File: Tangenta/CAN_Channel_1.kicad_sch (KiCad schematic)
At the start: 21 parts, among them J22 Conn_01x02_Pin, Q3 BSS138, U20 ADM3053

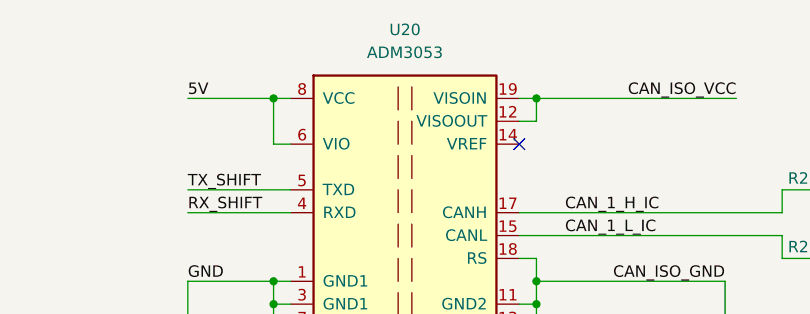
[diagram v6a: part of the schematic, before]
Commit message: Re-annotated. Ready for JLCPCB design verification.
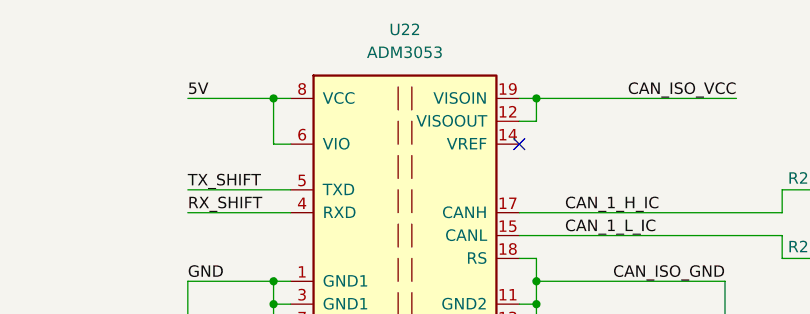
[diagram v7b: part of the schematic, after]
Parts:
- renumbered U20 to U22
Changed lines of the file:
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@@
         )
         (path "/358d1bcf-7599-4352-8c4d-baa18a5f09e6/b5394a48-5ef8-44c9-9d56-604d4ce6d7c8/96e01dc6-7803-4642-812e-1845a7add5da"
-          (reference "C189") (unit 1)
+          (reference "C199") (unit 1)
         )
       )
@@
         )
         (path "/358d1bcf-7599-4352-8c4d-baa18a5f09e6/b5394a48-5ef8-44c9-9d56-604d4ce6d7c8/96e01dc6-7803-4642-812e-1845a7add5da"
-          (reference "#PWR088") (unit 1)
+          (reference "#PWR094") (unit 1)
         )
       )
@@
         )
         (path "/358d1bcf-7599-4352-8c4d-baa18a5f09e6/b5394a48-5ef8-44c9-9d56-604d4ce6d7c8/96e01dc6-7803-4642-812e-1845a7add5da"
-          (reference "C195") (unit 1)
+          (reference "C202") (unit 1)
         )
       )
@@
         )
         (path "/358d1bcf-7599-4352-8c4d-baa18a5f09e6/b5394a48-5ef8-44c9-9d56-604d4ce6d7c8/96e01dc6-7803-4642-812e-1845a7add5da"
-          (reference "C188") (unit 1)
+          (reference "C197") (unit 1)
         )
       )
@@
         )
         (path "/358d1bcf-7599-4352-8c4d-baa18a5f09e6/b5394a48-5ef8-44c9-9d56-604d4ce6d7c8/96e01dc6-7803-4642-812e-1845a7add5da"
-          (reference "C191") (unit 1)
+          (reference "C200") (unit 1)
         )
       )
@@
         )
         (path "/358d1bcf-7599-4352-8c4d-baa18a5f09e6/b5394a48-5ef8-44c9-9d56-604d4ce6d7c8/96e01dc6-7803-4642-812e-1845a7add5da"
-          (reference "Q15") (unit 1)
+          (reference "Q19") (unit 1)
         )
       )
@@
         )
         (path "/358d1bcf-7599-4352-8c4d-baa18a5f09e6/b5394a48-5ef8-44c9-9d56-604d4ce6d7c8/96e01dc6-7803-4642-812e-1845a7add5da"
-          (reference "R151") (unit 1)
+          (reference "R190") (unit 1)
         )
       )
@@
         )
         (path "/358d1bcf-7599-4352-8c4d-baa18a5f09e6/b5394a48-5ef8-44c9-9d56-604d4ce6d7c8/96e01dc6-7803-4642-812e-1845a7add5da"
-          (reference "C193") (unit 1)
+          (reference "C201") (unit 1)
         )
       )
@@
         )
         (path "/358d1bcf-7599-4352-8c4d-baa18a5f09e6/b5394a48-5ef8-44c9-9d56-604d4ce6d7c8/96e01dc6-7803-4642-812e-1845a7add5da"
-          (reference "C192") (unit 1)
+          (reference "C203") (unit 1)
         )
       )
@@
         )
         (path "/358d1bcf-7599-4352-8c4d-baa18a5f09e6/b5394a48-5ef8-44c9-9d56-604d4ce6d7c8/96e01dc6-7803-4642-812e-1845a7add5da"
-          (reference "J23") (unit 1)
+          (reference "J32") (unit 1)
         )
       )
@@
         )
         (path "/358d1bcf-7599-4352-8c4d-baa18a5f09e6/b5394a48-5ef8-44c9-9d56-604d4ce6d7c8/96e01dc6-7803-4642-812e-1845a7add5da"
-          (reference "Q16") (unit 1)
+          (reference "Q20") (unit 1)
         )
       )
@@
         )
         (path "/358d1bcf-7599-4352-8c4d-baa18a5f09e6/b5394a48-5ef8-44c9-9d56-604d4ce6d7c8/96e01dc6-7803-4642-812e-1845a7add5da"
-          (reference "#PWR086") (unit 1)
+          (reference "#PWR093") (unit 1)
         )
       )
@@
         )
         (path "/358d1bcf-7599-4352-8c4d-baa18a5f09e6/b5394a48-5ef8-44c9-9d56-604d4ce6d7c8/96e01dc6-7803-4642-812e-1845a7add5da"
-          (reference "C190") (unit 1)
+          (reference "C198") (unit 1)
         )
       )
@@
         )
         (path "/358d1bcf-7599-4352-8c4d-baa18a5f09e6/b5394a48-5ef8-44c9-9d56-604d4ce6d7c8/96e01dc6-7803-4642-812e-1845a7add5da"
-          (reference "R177") (unit 1)
+          (reference "R189") (unit 1)
         )
       )
@@
         )
         (path "/358d1bcf-7599-4352-8c4d-baa18a5f09e6/b5394a48-5ef8-44c9-9d56-604d4ce6d7c8/96e01dc6-7803-4642-812e-1845a7add5da"
-          (reference "#PWR087") (unit 1)
+          (reference "#PWR092") (unit 1)
         )
       )
@@
         )
         (path "/358d1bcf-7599-4352-8c4d-baa18a5f09e6/b5394a48-5ef8-44c9-9d56-604d4ce6d7c8/96e01dc6-7803-4642-812e-1845a7add5da"
-          (reference "R168") (unit 1)
+          (reference "R191") (unit 1)
         )
       )
@@
         )
         (path "/358d1bcf-7599-4352-8c4d-baa18a5f09e6/b5394a48-5ef8-44c9-9d56-604d4ce6d7c8/96e01dc6-7803-4642-812e-1845a7add5da"
-          (reference "R175") (unit 1)
+          (reference "R187") (unit 1)
         )
       )
@@
         )
         (path "/358d1bcf-7599-4352-8c4d-baa18a5f09e6/b5394a48-5ef8-44c9-9d56-604d4ce6d7c8/96e01dc6-7803-4642-812e-1845a7add5da"
-          (reference "C194") (unit 1)
+          (reference "C204") (unit 1)
         )
       )
@@
         )
         (path "/358d1bcf-7599-4352-8c4d-baa18a5f09e6/b5394a48-5ef8-44c9-9d56-604d4ce6d7c8/96e01dc6-7803-4642-812e-1845a7add5da"
-          (reference "#PWR083") (unit 1)
+          (reference "#PWR091") (unit 1)
         )
       )
@@
         )
         (path "/358d1bcf-7599-4352-8c4d-baa18a5f09e6/b5394a48-5ef8-44c9-9d56-604d4ce6d7c8/96e01dc6-7803-4642-812e-1845a7add5da"
-          (reference "R176") (unit 1)
+          (reference "R188") (unit 1)
         )
       )
@@
         )
         (path "/358d1bcf-7599-4352-8c4d-baa18a5f09e6/b5394a48-5ef8-44c9-9d56-604d4ce6d7c8/96e01dc6-7803-4642-812e-1845a7add5da"
-          (reference "R184") (unit 1)
+          (reference "R192") (unit 1)
         )
       )
@@
   (symbol (lib_id "CholaSymbolsPrjLib:ADM3053") (at 137.16 74.93 0) (unit 1)
     (in_bom yes) (on_board yes) (dnp no) (fields_autoplaced)
-    (property "Reference" "U20" (at 137.16 52.07 0)
+    (property "Reference" "U22" (at 137.16 52.07 0)
       (effects (font (size 1.27 1.27)))
     )
@@
       (project "Tangenta"
         (path "/358d1bcf-7599-4352-8c4d-baa18a5f09e6/b5394a48-5ef8-44c9-9d56-604d4ce6d7c8/96e01dc6-7803-4642-812e-1845a7add5da"
-          (reference "U20") (unit 1)
+          (reference "U22") (unit 1)
         )
       )
@@
         )
         (path "/358d1bcf-7599-4352-8c4d-baa18a5f09e6/b5394a48-5ef8-44c9-9d56-604d4ce6d7c8/96e01dc6-7803-4642-812e-1845a7add5da"
-          (reference "R174") (unit 1)
-        )
-      )
+          (reference "R186") (unit 1)
+        )
+      )

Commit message: ...
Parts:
- C1: symbol CholaSymbolsPrjLib:C_Small -> LocalPrjLib:C_Small
- FB1: symbol CholaSymbolsPrjLib:GZ2012D101TF -> LocalPrjLib:GZ2012D101TF
- J22: symbol CholaSymbolsPrjLib:Conn_01x02_Pin -> LocalPrjLib:Conn_01x02_Pin
- Q3: symbol CholaSymbolsPrjLib:BSS138 -> LocalPrjLib:BSS138
- R2, R4: symbol CholaSymbolsPrjLib:R_Small_US -> LocalPrjLib:R_Small_US
- U22: symbol CholaSymbolsPrjLib:ADM3053 -> LocalPrjLib:ADM3053
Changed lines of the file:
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@@
     (effects (font (size 1.27 1.27)) (justify left))
   )
-  (symbol (lib_id "CholaSymbolsPrjLib:GZ2012D101TF") (at 168.91 140.97 0) (unit 1)
+  (symbol (lib_id "LocalPrjLib:GZ2012D101TF") (at 168.91 140.97 0) (unit 1)
     (in_bom yes) (on_board yes) (dnp no)
     (property "Reference" "FB1" (at 168.91 138.43 0)
@@
     )
   )
-  (symbol (lib_id "CholaSymbolsPrjLib:C_Small") (at 132.08 116.84 180) (unit 1)
+  (symbol (lib_id "LocalPrjLib:C_Small") (at 132.08 116.84 180) (unit 1)
     (in_bom yes) (on_board yes) (dnp no)
     (property "Reference" "C1" (at 129.5399 114.9349 0)
@@
     )
   )
-  (symbol (lib_id "CholaSymbolsPrjLib:C_Small") (at 159.385 135.89 0) (mirror x) (unit 1)
+  (symbol (lib_id "LocalPrjLib:C_Small") (at 159.385 135.89 0) (mirror x) (unit 1)
     (in_bom yes) (on_board yes) (dnp no)
     (property "Reference" "C1" (at 161.9251 133.9849 0)
@@
     )
   )
-  (symbol (lib_id "CholaSymbolsPrjLib:C_Small") (at 124.46 116.84 180) (unit 1)
+  (symbol (lib_id "LocalPrjLib:C_Small") (at 124.46 116.84 180) (unit 1)
     (in_bom yes) (on_board yes) (dnp no)
     (property "Reference" "C1" (at 121.9199 114.9349 0)
@@
     )
   )
-  (symbol (lib_id "CholaSymbolsPrjLib:C_Small") (at 132.08 135.89 180) (unit 1)
+  (symbol (lib_id "LocalPrjLib:C_Small") (at 132.08 135.89 180) (unit 1)
     (in_bom yes) (on_board yes) (dnp no)
     (property "Reference" "C1" (at 129.5399 133.9849 0)
@@
     )
   )
-  (symbol (lib_id "CholaSymbolsPrjLib:BSS138") (at 66.04 117.475 270) (unit 1)
+  (symbol (lib_id "LocalPrjLib:BSS138") (at 66.04 117.475 270) (unit 1)
     (in_bom yes) (on_board yes) (dnp no)
     (property "Reference" "Q3" (at 68.58 114.935 90)
@@
     )
   )
-  (symbol (lib_id "CholaSymbolsPrjLib:R_Small_US") (at 186.69 69.85 270) (unit 1)
+  (symbol (lib_id "LocalPrjLib:R_Small_US") (at 186.69 69.85 270) (unit 1)
     (in_bom yes) (on_board yes) (dnp no)
     (property "Reference" "R2" (at 179.705 68.58 90)
@@
     )
   )
-  (symbol (lib_id "CholaSymbolsPrjLib:C_Small") (at 141.605 116.84 0) (mirror x) (unit 1)
+  (symbol (lib_id "LocalPrjLib:C_Small") (at 141.605 116.84 0) (mirror x) (unit 1)
     (in_bom yes) (on_board yes) (dnp no)
     (property "Reference" "C1" (at 144.1451 114.9349 0)
@@
     )
   )
-  (symbol (lib_id "CholaSymbolsPrjLib:C_Small") (at 160.655 116.84 0) (mirror x) (unit 1)
+  (symbol (lib_id "LocalPrjLib:C_Small") (at 160.655 116.84 0) (mirror x) (unit 1)
     (in_bom yes) (on_board yes) (dnp no)
     (property "Reference" "C1" (at 163.1951 114.9349 0)
@@
     )
   )
-  (symbol (lib_id "CholaSymbolsPrjLib:Conn_01x02_Pin") (at 139.065 153.67 270) (unit 1)
+  (symbol (lib_id "LocalPrjLib:Conn_01x02_Pin") (at 139.065 153.67 270) (unit 1)
     (in_bom yes) (on_board yes) (dnp no)
     (property "Reference" "J22" (at 135.89 152.4 90)
@@
     )
   )
-  (symbol (lib_id "CholaSymbolsPrjLib:BSS138") (at 66.04 138.43 270) (unit 1)
+  (symbol (lib_id "LocalPrjLib:BSS138") (at 66.04 138.43 270) (unit 1)
     (in_bom yes) (on_board yes) (dnp no)
     (property "Reference" "Q3" (at 68.58 135.89 90)
@@
     )
   )
-  (symbol (lib_id "CholaSymbolsPrjLib:C_Small") (at 124.46 135.89 180) (unit 1)
+  (symbol (lib_id "LocalPrjLib:C_Small") (at 124.46 135.89 180) (unit 1)
     (in_bom yes) (on_board yes) (dnp no)
     (property "Reference" "C1" (at 121.9199 133.9849 0)
@@
     )
   )
-  (symbol (lib_id "CholaSymbolsPrjLib:R_Small_US") (at 80.01 134.62 180) (unit 1)
+  (symbol (lib_id "LocalPrjLib:R_Small_US") (at 80.01 134.62 180) (unit 1)
     (in_bom yes) (on_board yes) (dnp no)
     (property "Reference" "R2" (at 78.74 133.35 0)
@@
     )
   )
-  (symbol (lib_id "CholaSymbolsPrjLib:R_Small_US") (at 186.69 77.47 270) (unit 1)
+  (symbol (lib_id "LocalPrjLib:R_Small_US") (at 186.69 77.47 270) (unit 1)
     (in_bom yes) (on_board yes) (dnp no)
     (property "Reference" "R2" (at 179.705 76.2 90)
@@
     )
   )
-  (symbol (lib_id "CholaSymbolsPrjLib:R_Small_US") (at 53.34 134.62 180) (unit 1)
+  (symbol (lib_id "LocalPrjLib:R_Small_US") (at 53.34 134.62 180) (unit 1)
     (in_bom yes) (on_board yes) (dnp no)
     (property "Reference" "R2" (at 52.07 133.35 0)
@@
     )
   )
-  (symbol (lib_id "CholaSymbolsPrjLib:C_Small") (at 178.435 135.89 0) (mirror x) (unit 1)
+  (symbol (lib_id "LocalPrjLib:C_Small") (at 178.435 135.89 0) (mirror x) (unit 1)
     (in_bom yes) (on_board yes) (dnp no)
     (property "Reference" "C1" (at 180.9751 133.9849 0)
@@
     )
   )
-  (symbol (lib_id "CholaSymbolsPrjLib:R_Small_US") (at 80.01 113.665 180) (unit 1)
+  (symbol (lib_id "LocalPrjLib:R_Small_US") (at 80.01 113.665 180) (unit 1)
     (in_bom yes) (on_board yes) (dnp no)
     (property "Reference" "R2" (at 78.74 112.395 0)
@@
     )
   )
-  (symbol (lib_id "CholaSymbolsPrjLib:R_Small_US") (at 193.675 73.66 0) (unit 1)
+  (symbol (lib_id "LocalPrjLib:R_Small_US") (at 193.675 73.66 0) (unit 1)
     (in_bom yes) (on_board yes) (dnp no)
     (property "Reference" "R4" (at 197.485 72.39 0)
@@
     )
   )
-  (symbol (lib_id "CholaSymbolsPrjLib:ADM3053") (at 137.16 74.93 0) (unit 1)
+  (symbol (lib_id "LocalPrjLib:ADM3053") (at 137.16 74.93 0) (unit 1)
     (in_bom yes) (on_board yes) (dnp no) (fields_autoplaced)
     (property "Reference" "U22" (at 137.16 52.07 0)
@@
     )
   )
-  (symbol (lib_id "CholaSymbolsPrjLib:R_Small_US") (at 53.34 113.665 180) (unit 1)
+  (symbol (lib_id "LocalPrjLib:R_Small_US") (at 53.34 113.665 180) (unit 1)
     (in_bom yes) (on_board yes) (dnp no)
     (property "Reference" "R2" (at 52.07 112.395 0)
@@
     )
   )
-  (symbol (lib_id "CholaSymbolsPrjLib:GZ2012D101TF") (at 168.91 130.81 0) (unit 1)
+  (symbol (lib_id "LocalPrjLib:GZ2012D101TF") (at 168.91 130.81 0) (unit 1)
     (in_bom yes) (on_board yes) (dnp no)
     (property "Reference" "FB1" (at 168.91 128.27 0)
